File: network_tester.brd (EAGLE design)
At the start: 60.6 x 69.8 mm, 55 parts, among them SW1 SPST_TACT-KMR2, U1 Joystick, U2 RN2483, U3 ATSAMD21G-A, U5 MCP1640, X3 32.768, X4 microUSB

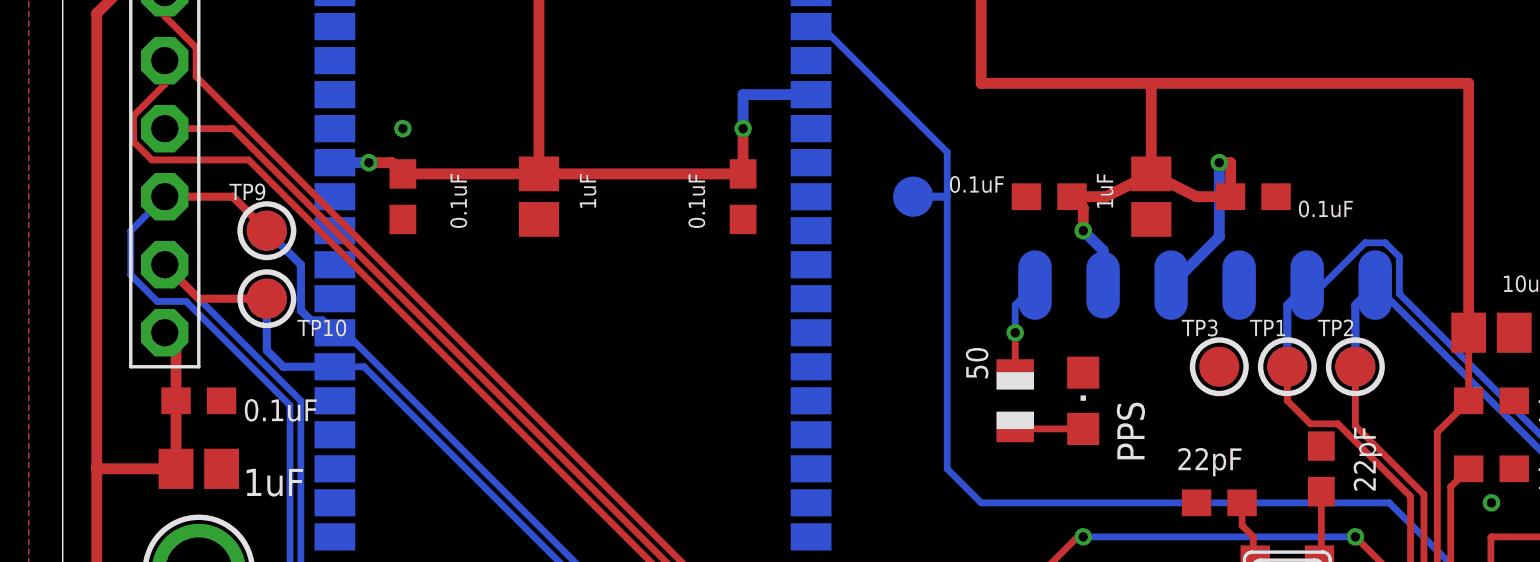
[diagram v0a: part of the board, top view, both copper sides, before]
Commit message: test point resolved
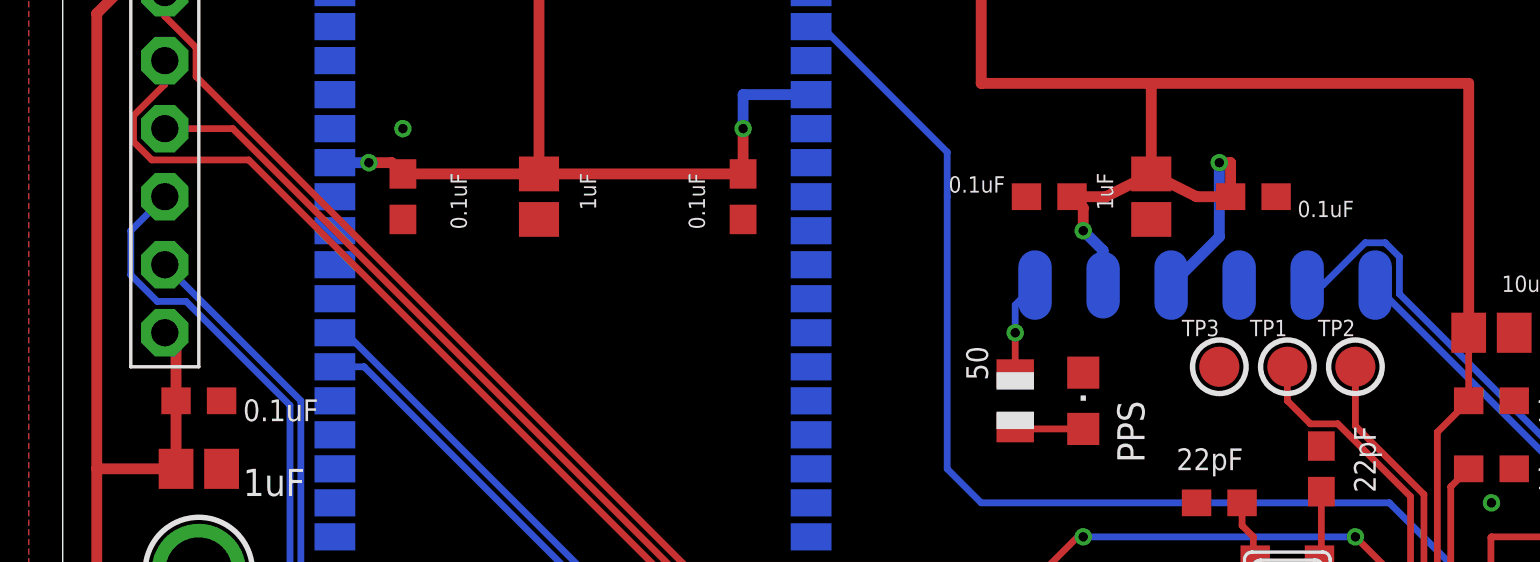
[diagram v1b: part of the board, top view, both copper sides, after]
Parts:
- removed TP10, TP14, TP5, TP6, TP7, TP8, TP9: (no value), Adafruit Feather M0 Basic rev C:TESTPOINT_ROUND_1.5MM
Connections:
- net MOSI: no longer TP9.P$1
- net RN2483_RESET: no longer TP14.P$1
- net SCK: no longer TP10.P$1
- net UART_GPS_RX: no longer TP7.P$1
- net UART_GPS_TX: no longer TP8.P$1
- net UART_RN2483_RX: no longer TP6.P$1
- net UART_RN2483_TX: no longer TP5.P$1
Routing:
- net UART_RN2483_TX: track 57.6 -> 52.4 mm
- net UART_RN2483_RX: track 58.6 -> 53.9 mm
- net SCK: track 72.2 -> 67.8 mm
- net MOSI: track 86.9 -> 82.6 mm
- net UART_GPS_RX: track 34.0 -> 30.6 mm
- net UART_GPS_TX: track 27.3 -> 24.0 mm
- net RN2483_RESET: track 50.0 -> 48.8 mm
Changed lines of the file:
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@@
 <grid distance="50" unitdist="mil" unit="mil" style="lines" multiple="1" display="no" altdistance="5" altunitdist="mil" altunit="mil"/>
 <layers>
-<layer number="1" name="Top" color="4" fill="1" visible="yes" active="yes"/>
+<layer number="1" name="Top" color="4" fill="1" visible="no" active="yes"/>
 <layer number="2" name="Route2" color="1" fill="3" visible="yes" active="yes"/>
 <layer number="3" name="Route3" color="4" fill="3" visible="yes" active="yes"/>
@@
 <attribute name="VALUE" x="15.113" y="12.065" size="0.4064" layer="27" ratio="10"/>
 </element>
-<element name="TP5" library="Adafruit Feather M0 Basic rev C" package="TESTPOINT_ROUND_1.5MM" value="" x="7.62" y="46.99" smashed="yes" rot="MR0">
-<attribute name="NAME" x="7.747" y="48.133" size="0.6096" layer="26" ratio="18" rot="MR0"/>
-<attribute name="VALUE" x="6.477" y="46.355" size="0.4064" layer="28" ratio="10" rot="MR0"/>
-</element>
-<element name="TP6" library="Adafruit Feather M0 Basic rev C" package="TESTPOINT_ROUND_1.5MM" value="" x="7.62" y="44.45" smashed="yes" rot="MR0">
-<attribute name="NAME" x="7.747" y="45.593" size="0.6096" layer="26" ratio="18" rot="MR0"/>
-<attribute name="VALUE" x="6.477" y="43.815" size="0.4064" layer="28" ratio="10" rot="MR0"/>
-</element>
-<element name="TP7" library="Adafruit Feather M0 Basic rev C" package="TESTPOINT_ROUND_1.5MM" value="" x="45.72" y="41.91" smashed="yes" rot="MR0">
-<attribute name="NAME" x="45.847" y="43.053" size="0.6096" layer="26" ratio="18" rot="MR0"/>
-<attribute name="VALUE" x="44.577" y="41.275" size="0.4064" layer="28" ratio="10" rot="MR0"/>
-</element>
-<element name="TP8" library="Adafruit Feather M0 Basic rev C" package="TESTPOINT_ROUND_1.5MM" value="" x="48.26" y="41.91" smashed="yes" rot="MR0">
-<attribute name="NAME" x="48.387" y="43.053" size="0.6096" layer="26" ratio="18" rot="MR0"/>
-<attribute name="VALUE" x="47.117" y="41.275" size="0.4064" layer="28" ratio="10" rot="MR0"/>
-</element>
-<element name="TP9" library="Adafruit Feather M0 Basic rev C" package="TESTPOINT_ROUND_1.5MM" value="" x="7.62" y="46.99" smashed="yes">
-<attribute name="NAME" x="6.223" y="48.133" size="0.6096" layer="25" ratio="18"/>
-<attribute name="VALUE" x="8.763" y="46.355" size="0.4064" layer="27" ratio="10"/>
-</element>
-<element name="TP10" library="Adafruit Feather M0 Basic rev C" package="TESTPOINT_ROUND_1.5MM" value="" x="7.62" y="44.45" smashed="yes">
-<attribute name="NAME" x="8.763" y="43.053" size="0.6096" layer="25" ratio="18"/>
-<attribute name="VALUE" x="8.763" y="43.815" size="0.4064" layer="27" ratio="10"/>
-</element>
-<element name="TP14" library="Adafruit Feather M0 Basic rev C" package="TESTPOINT_ROUND_1.5MM" value="" x="31.75" y="48.26" smashed="yes" rot="MR0">
-<attribute name="NAME" x="31.877" y="49.403" size="0.6096" layer="26" ratio="18" rot="MR0"/>
-<attribute name="VALUE" x="30.607" y="47.625" size="0.4064" layer="28" ratio="10" rot="MR0"/>
-</element>
 </elements>
 <signals>
@@
 <wire x1="58.5883375" y1="37.2364" x2="59.0268" y2="36.7979375" width="0.254" layer="16"/>
 <wire x1="59.0268" y1="36.7979375" x2="59.0268" y2="27.68865" width="0.254" layer="16"/>
-<contactref element="TP7" pad="P$1"/>
-<wire x1="46.46" y1="44.96" x2="45.72" y2="44.22" width="0.3048" layer="16"/>
-<wire x1="45.72" y1="44.22" x2="45.72" y2="41.91" width="0.3048" layer="16"/>
 </signal>
 <signal name="N$1">
@@
 <wire x1="49.53" y1="36.83" x2="52.07" y2="34.29" width="0.254" layer="16"/>
 <wire x1="52.07" y1="34.29" x2="52.07" y2="30.48" width="0.254" layer="16"/>
-<contactref element="TP14" pad="P$1"/>
-<wire x1="31.75" y1="48.26" x2="33.02" y2="48.26" width="0.3048" layer="16"/>
 </signal>
 <signal name="TFT_RST">
@@
 <wire x1="58.42" y1="27.94" x2="57.94" y2="27.46" width="0.254" layer="1"/>
 <wire x1="57.94" y1="27.46" x2="56.32" y2="27.46" width="0.254" layer="1"/>
-<contactref element="TP8" pad="P$1"/>
-<wire x1="49" y1="44.96" x2="48.26" y2="44.22" width="0.3048" layer="16"/>
-<wire x1="48.26" y1="44.22" x2="48.26" y2="41.91" width="0.3048" layer="16"/>
 </signal>
 <signal name="SCK">
@@
 <wire x1="52.07" y1="22.1647375" x2="52.07" y2="22.86" width="0.254" layer="16"/>
 <wire x1="35.99043125" y1="19.4564" x2="49.3616625" y2="19.4564" width="0.254" layer="16"/>
-<contactref element="TP10" pad="P$1"/>
-<wire x1="7.62" y1="44.45" x2="5.08" y2="44.45" width="0.3048" layer="1"/>
-<wire x1="5.08" y1="44.45" x2="3.81" y2="45.72" width="0.3048" layer="1"/>
 </signal>
 <signal name="MOSI">
@@
 <wire x1="50.8" y1="27.94" x2="52.32" y2="27.94" width="0.254" layer="1"/>
 <wire x1="52.32" y1="27.94" x2="52.32" y2="24.96" width="0.254" layer="1"/>
-<contactref element="TP9" pad="P$1"/>
-<wire x1="7.62" y1="46.99" x2="6.35" y2="48.26" width="0.3048" layer="1"/>
-<wire x1="6.35" y1="48.26" x2="3.81" y2="48.26" width="0.3048" layer="1"/>
 </signal>
 <signal name="UART_RN2483_RX">
@@
 <wire x1="37.6936" y1="30.8864" x2="37.6936" y2="27.7716625" width="0.254" layer="16"/>
 <wire x1="21.81679375" y1="31.3436" x2="37.2364" y2="31.3436" width="0.254" layer="16"/>
-<contactref element="TP6" pad="P$1"/>
-<wire x1="10.16" y1="41.91" x2="8.2306625" y2="41.91" width="0.3048" layer="16"/>
-<wire x1="7.62" y1="42.5206625" x2="7.62" y2="44.45" width="0.3048" layer="16"/>
-<wire x1="8.2306625" y1="41.91" x2="7.62" y2="42.5206625" width="0.3048" layer="16"/>
 </signal>
 <signal name="UART_RN2483_TX">
@@
 <wire x1="10.55513125" y1="43.18" x2="10.16" y2="43.18" width="0.254" layer="16"/>
 <wire x1="10.55513125" y1="43.18" x2="21.98513125" y2="31.75" width="0.254" layer="16"/>
-<contactref element="TP5" pad="P$1"/>
-<wire x1="10.16" y1="43.18" x2="9.7028" y2="43.6372" width="0.3048" layer="16"/>
-<wire x1="9.7028" y1="43.6372" x2="9.27175" y2="43.6372" width="0.3048" layer="16"/>
-<wire x1="9.27175" y1="43.6372" x2="8.89" y2="44.01895" width="0.3048" layer="16"/>
-<wire x1="8.89" y1="44.01895" x2="8.89" y2="45.72" width="0.3048" layer="16"/>
-<wire x1="8.89" y1="45.72" x2="7.62" y2="46.99" width="0.3048" layer="16"/>
 </signal>
 <signal name="N$5">

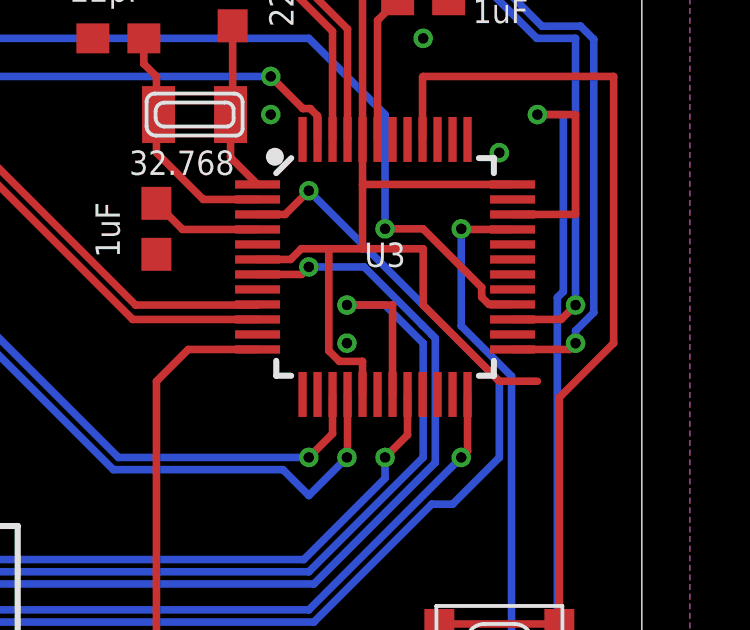
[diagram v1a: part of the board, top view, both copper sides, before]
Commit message: test point resolved
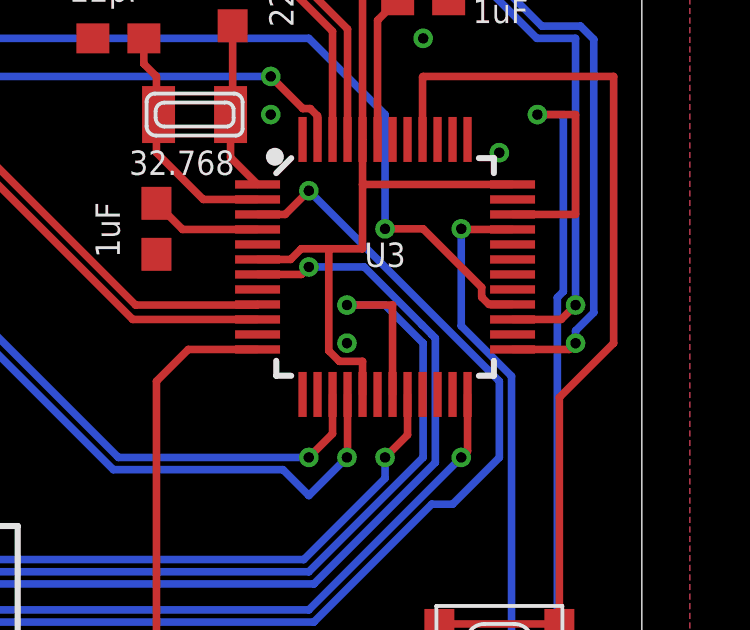
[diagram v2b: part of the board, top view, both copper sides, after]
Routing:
- net 3V: track 260.9 -> 252.1 mm
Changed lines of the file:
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@@
 <grid distance="50" unitdist="mil" unit="mil" style="lines" multiple="1" display="no" altdistance="5" altunitdist="mil" altunit="mil"/>
 <layers>
-<layer number="1" name="Top" color="4" fill="1" visible="no" active="yes"/>
+<layer number="1" name="Top" color="4" fill="1" visible="yes" active="yes"/>
 <layer number="2" name="Route2" color="1" fill="3" visible="yes" active="yes"/>
 <layer number="3" name="Route3" color="4" fill="3" visible="yes" active="yes"/>
@@
 <wire x1="50.1932" y1="26.41865" x2="50.1932" y2="29.8168" width="0.254" layer="1"/>
 <wire x1="51.32" y1="31.96" x2="56.32" y2="31.96" width="0.254" layer="1"/>
-<wire x1="57.15" y1="25.4" x2="55.88" y2="25.4" width="0.254" layer="1"/>
-<wire x1="55.88" y1="25.4" x2="53.34" y2="27.94" width="0.254" layer="1"/>
-<wire x1="53.34" y1="27.94" x2="53.34" y2="29.8168" width="0.254" layer="1"/>
-<wire x1="53.34" y1="29.8168" x2="51.32" y2="29.8168" width="0.254" layer="1"/>
 <wire x1="7.62" y1="30.48" x2="1.27" y2="30.48" width="0.4064" layer="1"/>
 <contactref element="U5" pad="5"/>

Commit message: First commit of board for external fabbing -- untested
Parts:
- removed PPS: (no value), adafruit:CHIPLED_0805
- removed SW1: SPST_TACT-KMR2, adafruit:KMR2
- removed X3: 32.768, Adafruit Feather M0 Basic rev C:XTAL3215
- added C20, C22, C23: 100nf, Seeed-Capacitor:C0402
- added D1: RED-0805, Seeed-LED:LED-0805
- added SW2: DHT-4235A, Seeed-Switch:SW4-SMD-4.2X3.2X2.5MM
- added Y1: 32.768, Seeed-Crystal Oscillator:X2-SMD-L2.0X1.2X0.55MM
- C1, C12, C14, C15, C19, C2, C21, C9: value 0.1uF -> 100nf; device adafruit:C0603 -> Seeed-Capacitor:C0402
- C10: value 4.7uF -> 4.7uf; device SparkFun:0805 -> Seeed-Capacitor:C0402
- C11: value 10uF -> 10uf; device SparkFun:0805 -> Seeed-Capacitor:C0402
- C13: value 10uF -> 10uf; device adafruit:C0805 -> Seeed-Capacitor:C0402
- C16: value 1uF -> 1UF; device adafruit:C0805 -> Seeed-Capacitor:C0402
- C17, C7: value 1uF -> 1UF; device adafruit:C0603 -> Seeed-Capacitor:C0402
- C18, C3, C8: value 1uF -> 1UF 6.3V; device adafruit:C0805 -> Seeed-Capacitor:C0402
- C4, C5: value 22pF -> 22pf; device adafruit:C0603 -> Seeed-Capacitor:C0402
- C6: value 1uF -> 1UF 6.3V; device adafruit:C0603 -> Seeed-Capacitor:C0402
- U3: value ATSAMD21G-A -> ATSAMD21G-M; device Albert-Arduino:TQFP-48 -> Albert-Arduino:QFN-48
- X4: value microUSB -> ZX62-B-5PA; device microbuilder:4UCONN_20329_V2 -> Seeed-Connector:MICRO-USB5+6P-SMD-0.65-AB
- moved C13 5.24 mm to (52.1, 38.1), turned to 90 degrees
- moved C17 4.02 mm to (52.1, 36.8), turned to 90 degrees
- moved C7 4.02 mm to (52.1, 34.3), turned to 180 degrees
- moved C16 4.02 mm to (15.2, 22.9), turned to 270 degrees
- moved C5 3.81 mm to (47.0, 34.3)
- moved C15 2.84 mm to (25.4, 6.35), turned to 0 degrees
- moved C4 2.84 mm to (44.5, 34.3), turned to 270 degrees
- moved C14 2.84 mm to (20.3, 21.6)
- moved C2 2.54 mm to (41.9, 48.3)
- moved X4 2.54 mm to (49.5, 1.83)
- moved C1 2.54 mm to (39.4, 48.3), turned to 0 degrees
- moved C6 1.80 mm to (43.2, 31.8), turned to 180 degrees
- moved C18 1.80 mm to (3.81, 39.4), turned to 90 degrees
- moved C21 1.27 mm to (7.62, 59.7)
- moved C19 1.27 mm to (3.81, 40.6), turned to 90 degrees
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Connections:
- net 3V: now also C20.2, C22.1, C23.1
- net D+: now also X4.3; no longer X4.D+
- net D-: now also X4.2; no longer X4.D-
- net GND: now also C20.1, C22.2, C23.2, C7.2, D1.-, SW2.4, X4.5, X4.P1, X4.P2, X4.P3_1, X4.P3_2, X4.P3_3, X4.P4_1, X4.P4_2, X4.P4_3, X4.P5, X4.P6; no longer PPS.C, SW1.2, SW1.4, X4.BASE@1, X4.BASE@2, X4.GND, X4.SPRT@1, X4.SPRT@2, X4.SPRT@3, X4.SPRT@4
- net N$2: now also D1.+; no longer PPS.A
- net N$3: now also Y1.1; no longer X3.P$1
- net N$7: now also Y1.2; no longer X3.P$2
- net RESET: now also SW2.1; no longer SW1.1, SW1.3
- net VBUS: now also X4.1; no longer X4.VBUS
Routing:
- net VRY: track 47.3 -> 71.7 mm, vias 1 -> 5
- net TFT_CS: track 57.8 -> 75.7 mm, vias 2 -> 1
- net RESET: track 31.5 -> 17.2 mm, vias 0 -> 2
- net SW: track 39.6 -> 53.7 mm
- net VRX: track 50.3 -> 38.6 mm, vias 1 -> 2
- net D+: track 41.7 -> 32.6 mm, vias 2 -> 0
- net GND: track 6.68 -> 15.8 mm, vias 71 -> 81
- net MOSI: track 82.6 -> 74.6 mm
- net 3V: track 252.1 -> 259.9 mm, vias 6 -> 9
- net UART_RN2483_RX: track 53.9 -> 49.2 mm
- net UART_RN2483_TX: track 52.4 -> 48.3 mm
- net N$4: track 4.92 -> 1.27 mm
- net SCK: track 67.8 -> 70.6 mm, vias 1 -> 2
- net N$3: track 8.10 -> 5.94 mm
- net RN2483_RESET: track 48.8 -> 50.9 mm, vias 1 -> 3
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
